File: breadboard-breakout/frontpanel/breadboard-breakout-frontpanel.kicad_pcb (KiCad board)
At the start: 2 copper layers, 40.3 x 128.5 mm, 15 parts

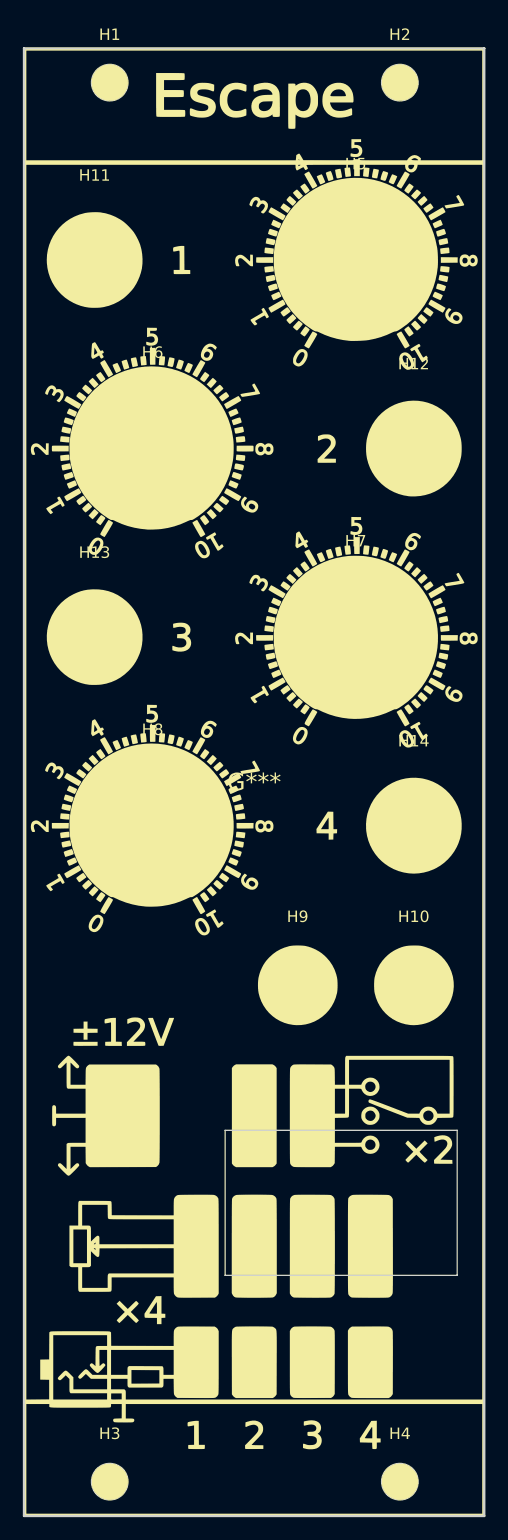
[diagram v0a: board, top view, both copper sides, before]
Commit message: breakout: Finalize the frontpanel
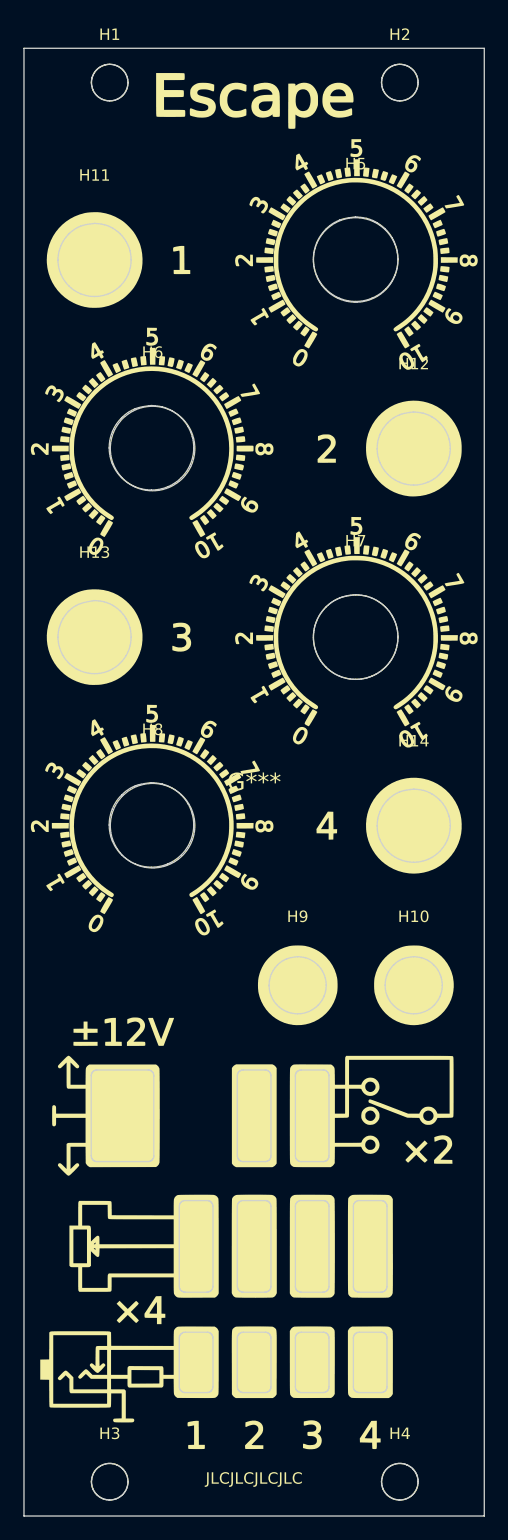
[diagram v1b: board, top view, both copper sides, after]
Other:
- outline, holes or cut-outs redrawn
- board text added: "JLCJLCJLCJLC"

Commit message: breakout: Add a copper layer
Add a copper layer spanning the whole board.
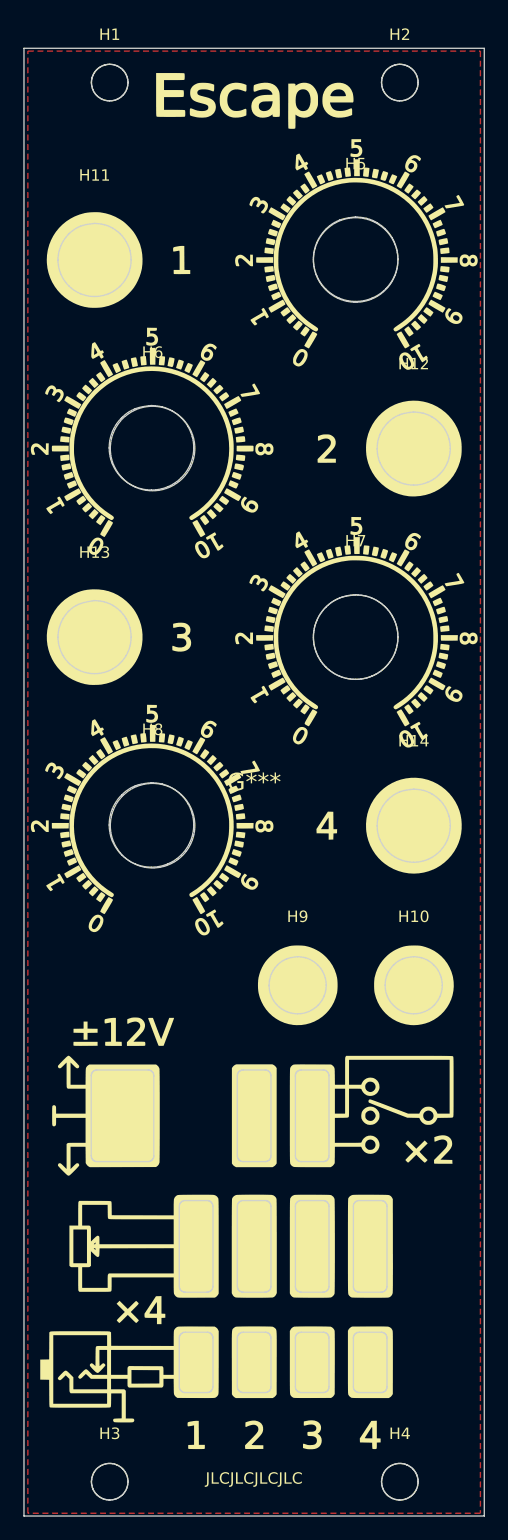
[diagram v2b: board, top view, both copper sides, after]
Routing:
- added copper zone on F.Cu, net (none)
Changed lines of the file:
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@@
     (effects (font (size 1 1) (thickness 0.15)))
+  )
+  (zone (net 0) (net_name "") (layer "F.Cu") (hatch edge 0.508)
+    (connect_pads (clearance 0.508))
+    (min_thickness 0.254) (filled_areas_thickness no)
+    (fill yes (thermal_gap 0.508) (thermal_bridge_width 0.508))
+    (polygon
+      (pts
+        (xy 19.812 64.008)
+        (xy -19.812 64.008)
+        (xy -19.812 -64.008)
+        (xy 19.812 -64.008)
+      )
+    )
   )
   (group "" (id f217d6dd-7d0a-491c-b306-286edc3a63cf)
